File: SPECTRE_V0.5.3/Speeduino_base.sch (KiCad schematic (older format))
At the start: 218 parts, among them J1 Conn_01x06_Male, J2 Conn_02x04_Odd_Even, J3 ProtoArea, Q1 AO3400, Q10 BSP78, Q11 BSP78, Q12 AO3400, Q13 BSP78, Q14 BSP78, Q15 BSP78, Q16 BSP78, Q17 BSP78, Q18 BSP78, Q19 BSP78, Q20 BSP78, Q21 BSP78, Q6 AO3400, Q7 AO3400, U1 MAX9926UAEE+, U10 MIC4427, U2 LM78M05_TO220, U3 TL431DBZ, U4 molex_48pin, U5 TJA1050, U6 MAX3232, U7 MIC4427, U8 MIC4427, U9 MIC4427

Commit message: Organization
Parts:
- Q1: symbol Speeduino_base-eagle-import:SMD-MOSFET-N-CH-60V-300MA-LOGIC-LEVEL-FET-2N7002(SOT-23) -> Speeduino_base-eagle-import:SMD-MOSFET-N-CH-20V-2.1A-CJ2302(SOT-23)
- U4: symbol molex_48pin:molex_48pin -> Speeduino_base-rescue:molex_48pin-molex_48pin
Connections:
- wire segments 570 -> 591
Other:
- moved on the sheet: A1, C1, C10, C11, C12, C13, C14, C15, C16, C17, C18, C19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

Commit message: Now with correct file/lib locations for the 48pin molex
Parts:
- removed U4: molex_48pin, rusefi_lib:Molex_48, symbol Speeduino_base-rescue:molex_48pin-molex_48pin
- added U?: molex_48pin, Speeduino_base:Molex_48, symbol molex_48pin:molex_48pin
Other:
- moved on the sheet: JP15, JP16, JP18, JP5, JP6, JP7, JP8

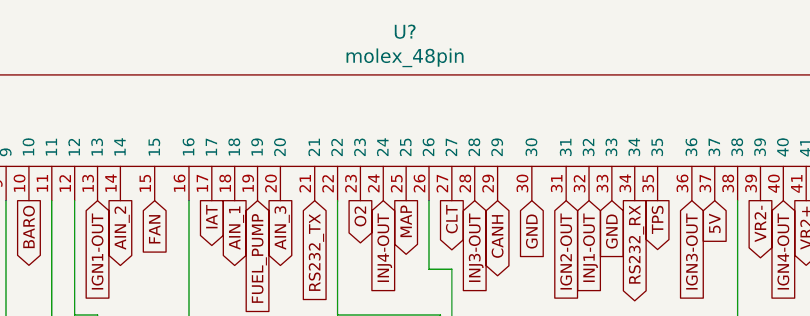
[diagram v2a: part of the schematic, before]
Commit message: update molex 48 pin to correct location
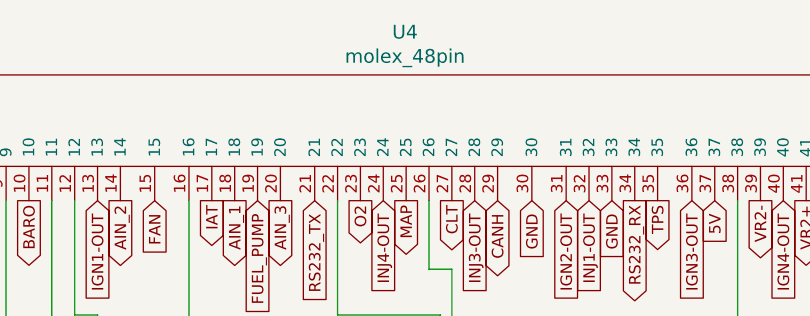
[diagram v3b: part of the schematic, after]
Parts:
- gave numbers to parts that had none: 1
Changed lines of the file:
@@
 Wire Wire Line
 	2950 6900 3900 6900
+Connection ~ 6550 1250
 $Comp
-L molex_48pin:molex_48pin U?
+L molex_48pin:molex_48pin U4
 U 1 1 5FFFB3E6
 P 9250 1800
-F 0 "U?" V 10537 2205 60  0000 C CNN
+F 0 "U4" V 10537 2205 60  0000 C CNN
 F 1 "molex_48pin" V 10431 2205 60  0000 C CNN
 F 2 "Speeduino_base:Molex_48" H 9250 1800 60  0001 C CNN
@@
 	0    -1   -1   0
 $EndComp
-Connection ~ 6550 1250
 $EndSCHEMATC

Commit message: Complete rework on PCB
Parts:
- removed R10, R26, R29, R47: 9k1, Speeduino_base:R0603, symbol Speeduino_base-eagle-import:R-EU_R0805
- removed R25, R28, R46, R9: 4k7, Speeduino_base:R0603, symbol Speeduino_base-eagle-import:R-EU_R0805
- removed R34, R56, R83, R85: 100R, Speeduino_base:R0603, symbol Speeduino_base-eagle-import:SMD-RES-470R-5%-1_10W(0603)
- removed R36, R59, R79, R80, R81, R82, R86, R88, R89, R90, R91, R92: 10k, Speeduino_base:R0603, symbol Speeduino_base-eagle-import:SMD-RES-470R-5%-1_10W(0603)
- removed R39, R40, R43, R48, R51, R52, R53, R54: 100R, Speeduino_base:R0603, symbol Device:R_Small
- added R25, R28, R46, R9: 4k7, Speeduino_base:R0603, symbol Speeduino_base-eagle-import:SMD-RES-470R-5%-1_10W(0603)
- added RN1, RN3, RN7: 100R, Resistor_SMD:R_Array_Convex_4x0612, symbol Device:R_Pack04_Split
- added RN2, RN4, RN8: 10K, Resistor_SMD:R_Array_Convex_4x0612, symbol Device:R_Pack04_Split
- added RN6: 9K1, Resistor_SMD:R_Array_Convex_4x0612, symbol Device:R_Pack04_Split
- R66, R87: value 10k -> 10K
- U4: symbol molex_48pin:molex_48pin -> Speeduino_base-rescue:molex_48pin-molex_48pin
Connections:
- wire segments 591 -> 603
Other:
- moved on the sheet: A1, C1, C10, C11, C13, C14, C16, C19, C2, C20, C21, C22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
